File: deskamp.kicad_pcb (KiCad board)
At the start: 2 copper layers, 38 parts, among them J1 Input 01, J10 Input Select, J2 Input 02, J3 Preamp Out, J5 LFE, J6 Mute, J7 Sleep, J8 Motor, J9 Power, K1 TQ2-12V, K2 TQ2-12V, K3 TQ2-12V, K4 TQ2-12V, Q1 PN2222A, Q2 PN2222A, Q3 PN2222A, Q4 PN2222A, U1 esp32-wemos-d1-mini, U2 L9110, U3 TSR_1-2433

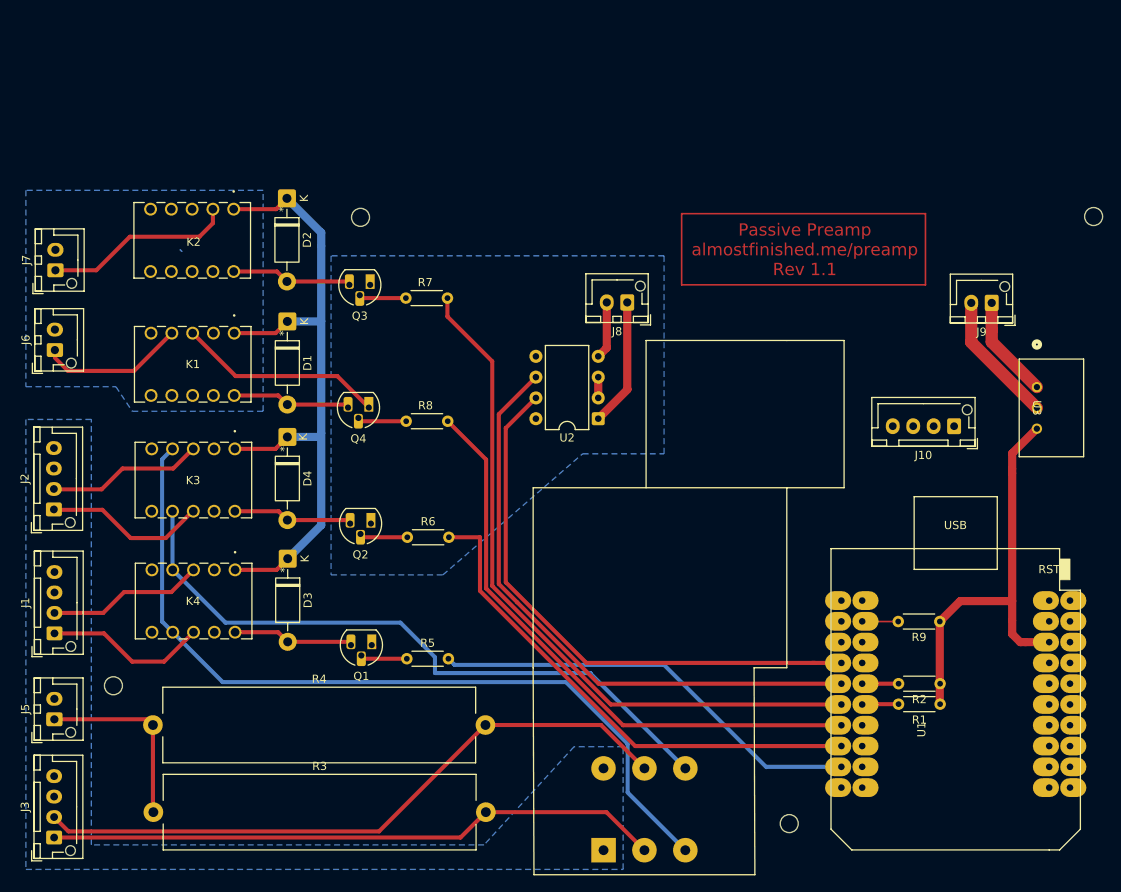
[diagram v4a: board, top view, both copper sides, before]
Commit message: Add board edge
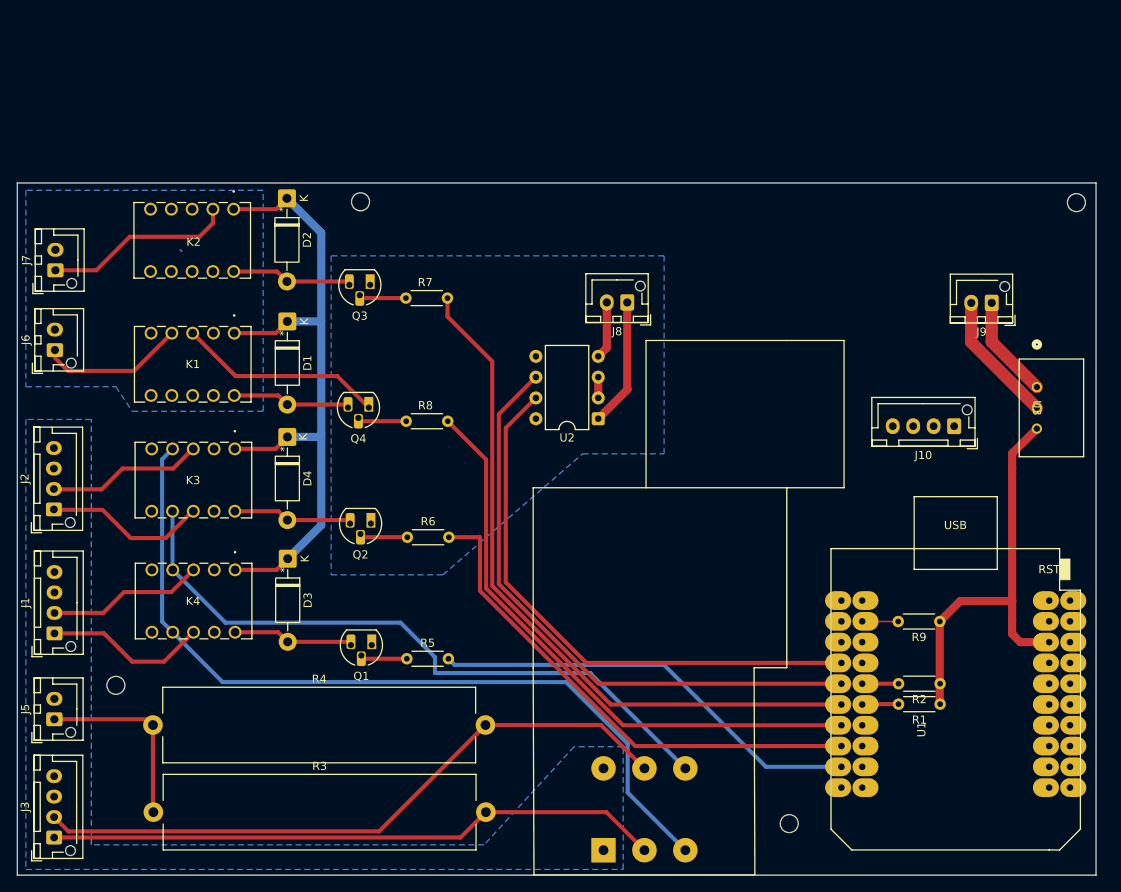
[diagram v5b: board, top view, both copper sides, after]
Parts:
- moved REF** 2.70 mm to (187.4, 65.5)
- moved REF** 1.90 mm to (99.9, 65.4)
- moved REF** 0.30 mm to (70.0, 124.5)
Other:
- board outline added: 131.9 x 84.6 mm
- board text removed: "Passive Preamp almostfinished.me/preamp Rev 1.1"

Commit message: Update deskamp.kicad_pcb
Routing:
- net +12V: track 96.7 -> 188.1 mm
- net GND: track 42.2 -> 131.4 mm
- net +3V3: track 54.0 -> 114.7 mm
- net Net-(J10-Pin_2): track 4.48 -> 40.2 mm
- net Net-(J10-Pin_3): track 4.44 -> 36.7 mm
- net Net-(J10-Pin_4): track 4.41 -> 28.6 mm
- net Net-(U1-IO_04): track 75.6 -> 74.1 mm
- net Net-(K3-Pad4): track 81.0 -> 79.9 mm

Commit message: Update deskamp.kicad_pcb
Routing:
- net Net-(J6-Pin_1): track 17.8 -> 15.2 mm
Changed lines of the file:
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@@
 			(at 2.54 1.92 0)
 			(layer "F.Fab")
+			(hide yes)
 			(effects
 				(font
@@
 			(at 2.54 1.92 0)
 			(layer "F.Fab")
+			(hide yes)
 			(effects
 				(font
@@
 	)
 	(segment
-		(start 167.29 68)
+		(start 89.583325 66.3)
+		(end 90.905825 64.9775)
+		(width 0.5)
+		(layer "F.Cu")
+		(net 1)
+	)
+	(segment
+		(start 90.905825 64.9775)
+		(end 94.928325 69)
+		(width 1)
+		(layer "F.Cu")
+		(net 1)
+	)
+	(segment
+		(start 168.29 69)
 		(end 177.045 77.755)
 		(width 1)
@@
 	)
 	(segment
-		(start 89.583325 66.3)
-		(end 90.905825 64.9775)
-		(width 0.5)
+		(start 94.928325 69)
+		(end 168.29 69)
+		(width 1)
 		(layer "F.Cu")
 		(net 1)
@@
 	)
 	(segment
-		(start 90.905825 64.9775)
-		(end 93.928325 68)
-		(width 1)
-		(layer "F.Cu")
-		(net 1)
-	)
-	(segment
 		(start 84.54 95.6)
 		(end 89.5 95.6)
@@
 	)
 	(segment
-		(start 93.928325 68)
-		(end 167.29 68)
-		(width 1)
-		(layer "F.Cu")
-		(net 1)
-	)
-	(segment
 		(start 95.1 69.171675)
 		(end 95.1 80)
@@
 	)
 	(segment
-		(start 174.545 77.755)
-		(end 169.245 77.755)
+		(start 149 98)
+		(end 127.425 98)
 		(width 1.5)
 		(layer "F.Cu")
@@
 	)
 	(segment
-		(start 149 98)
-		(end 127.425 98)
+		(start 169.245 77.755)
+		(end 149 98)
 		(width 1.5)
 		(layer "F.Cu")
@@
 	)
 	(segment
-		(start 174.545 82.568)
-		(end 174.545 77.755)
+		(start 174.545 77.755)
+		(end 169.245 77.755)
 		(width 1.5)
 		(layer "F.Cu")
@@
 	)
 	(segment
-		(start 169.245 77.755)
-		(end 149 98)
+		(start 174.545 82.568)
+		(end 174.545 77.755)
 		(width 1.5)
 		(layer "F.Cu")
@@
 	)
 	(segment
-		(start 72.219 86.071)
+		(start 74.77 83.52)
 		(end 76.84 81.45)
 		(width 0.5)
@@
 	)
 	(segment
-		(start 62.5427 84.464917)
-		(end 64.148783 86.071)
-		(width 0.5)
-		(layer "F.Cu")
-		(net 12)
-	)
-	(segment
 		(start 62.5427 83.52)
-		(end 62.5427 84.464917)
-		(width 0.2)
-		(layer "F.Cu")
-		(net 12)
-	)
-	(segment
-		(start 64.148783 86.071)
-		(end 72.219 86.071)
+		(end 74.77 83.52)
 		(width 0.5)
 		(layer "F.Cu")

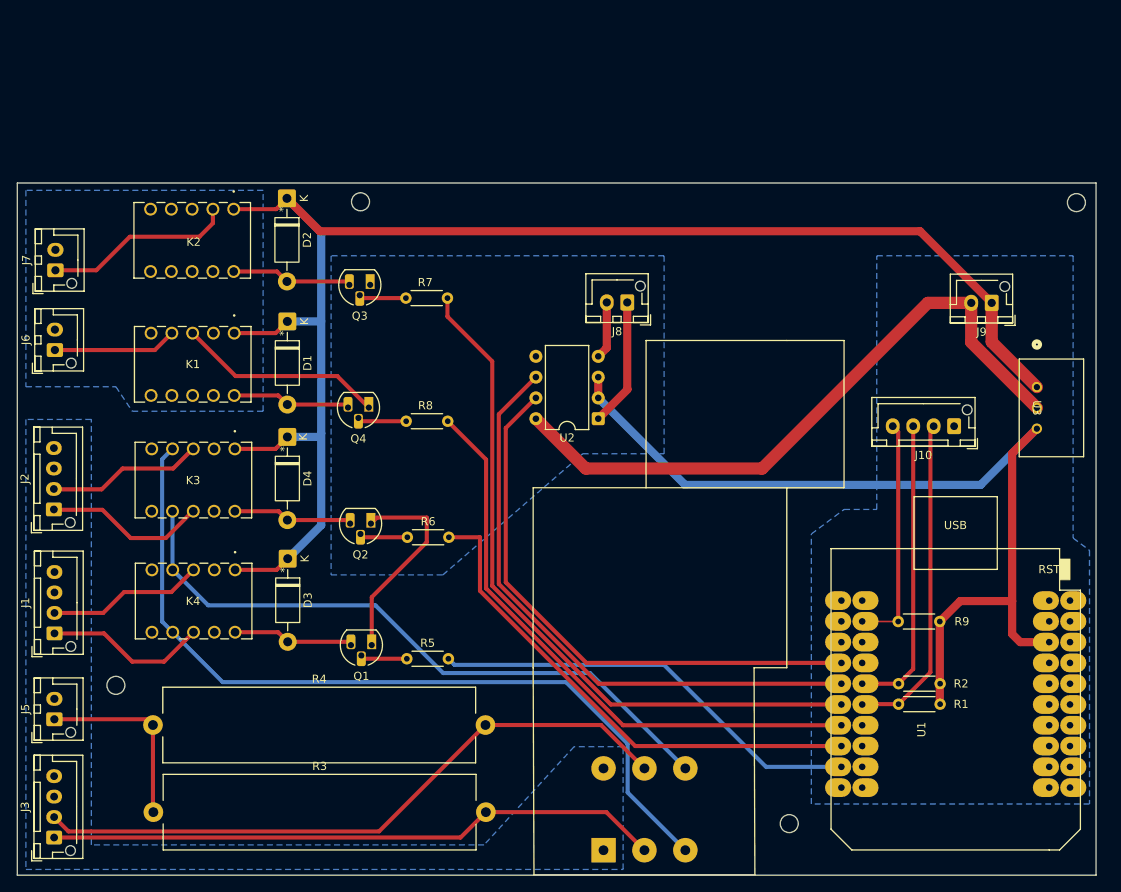
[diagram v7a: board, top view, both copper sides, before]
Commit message: Start afresh with layout
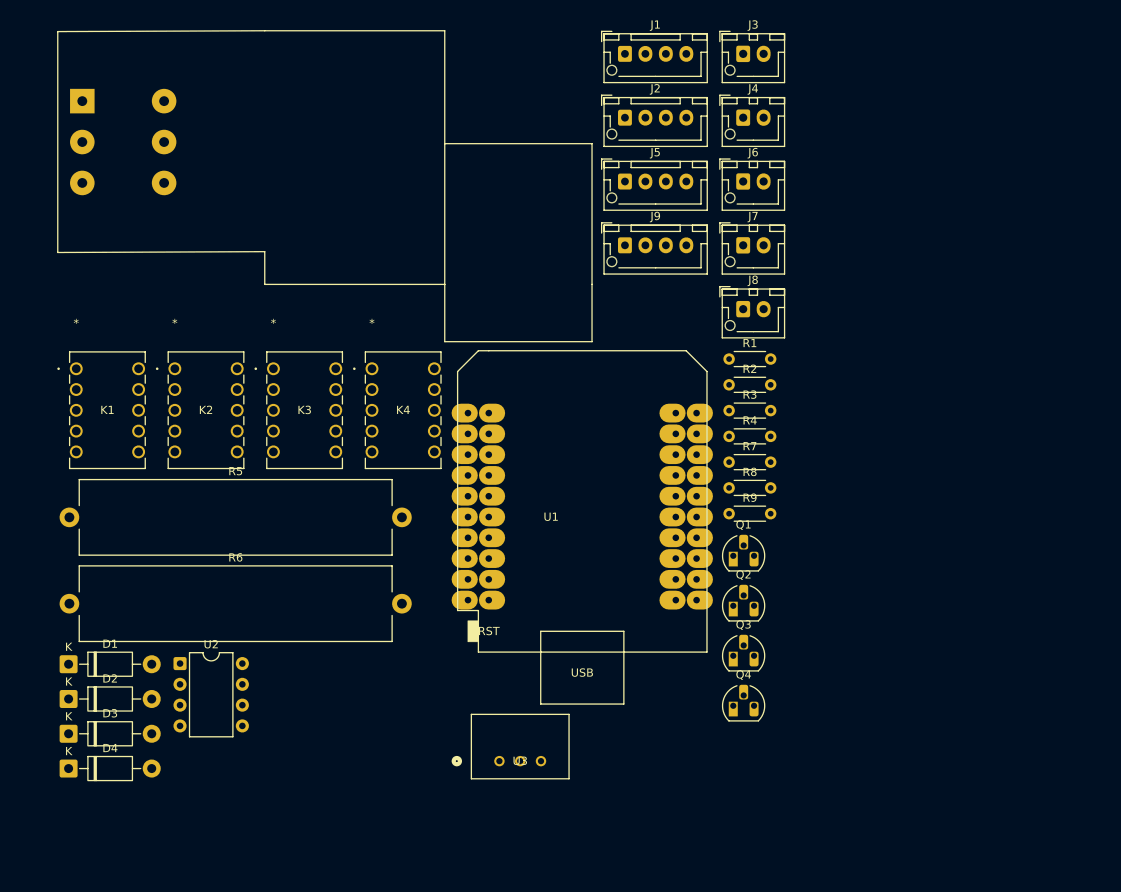
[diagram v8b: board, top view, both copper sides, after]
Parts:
- removed J10: Input Select, Connector_JST:JST_XH_B4B-XH-AM_1x04_P2.50mm_Vertical
- removed REF** (x4): MountingHole_2.2mm_M2_DIN965, MountingHole:MountingHole_2.2mm_M2_DIN965
- added J4: Mute, Connector_JST:JST_XH_B2B-XH-AM_1x02_P2.50mm_Vertical, F.Cu at (146.7, 55.1)
- J3: value Preamp Out -> Sleep; footprint Connector_JST:JST_XH_B4B-XH-AM_1x04_P2.50mm_Vertical -> Connector_JST:JST_XH_B2B-XH-AM_1x02_P2.50mm_Vertical
- J5: value LFE -> Preamp Out; footprint Connector_JST:JST_XH_B2B-XH-AM_1x02_P2.50mm_Vertical -> Connector_JST:JST_XH_B4B-XH-AM_1x04_P2.50mm_Vertical
- J6: value Mute -> LFE
- J7: value Sleep -> Power
- J9: value Power -> Input Select; footprint Connector_JST:JST_XH_B2B-XH-AM_1x02_P2.50mm_Vertical -> Connector_JST:JST_XH_B4B-XH-AM_1x04_P2.50mm_Vertical
- R1, R2: value 10K -> 1K
- R3, R4: value 10K -> 1K; footprint Resistor_THT:R_Axial_Power_L38.0mm_W9.0mm_P40.64mm -> Resistor_THT:R_Axial_DIN0204_L3.6mm_D1.6mm_P5.08mm_Horizontal
- R5, R6: value 1K -> 10K; footprint Resistor_THT:R_Axial_DIN0204_L3.6mm_D1.6mm_P5.08mm_Horizontal -> Resistor_THT:R_Axial_Power_L38.0mm_W9.0mm_P40.64mm
- R7, R8: value 1K -> 10K
- moved J3 127.5 mm to (146.7, 47.3), turned to 0 degrees
- moved RV1 112.9 mm to (64.9, 53.1), turned to 0 degrees
- moved J1 99.4 mm to (132.2, 47.3), turned to 0 degrees
- moved J5 95.8 mm to (132.2, 62.9), turned to 0 degrees
- moved J6 86.6 mm to (146.7, 62.9), turned to 0 degrees
- moved R3 85.8 mm to (144.9, 90.9)
- moved J2 84.6 mm to (132.2, 55.1), turned to 0 degrees
- moved J7 84.1 mm to (146.7, 70.7), turned to 0 degrees
- moved U3 80.0 mm to (116.9, 133.8), turned to 0 degrees
- moved R4 78.8 mm to (144.9, 94.1)
- moved D2 66.8 mm to (64.2, 126.2), turned to 0 degrees
- moved Q3 63.4 mm to (145.5, 120.9), turned to 0 degrees
- moved U2 59.2 mm to (77.8, 121.8), turned to 0 degrees
- moved Q4 57.6 mm to (145.5, 127.0), turned to 0 degrees
- moved U1 51.1 mm to (127.0, 102.7), turned to 0 degrees
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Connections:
- J3 pad 2: Net-(J3-Pin_2) -> GND
- J5 pad 2: GNDA -> Net-(J5-Pin_2)
- J6 pad 2: GND -> GNDA
- J7 pad 1: Net-(J7-Pin_1) -> +12V
- J9 pad 1: +12V -> GND
- J9 pad 2: GND -> Net-(J9-Pin_2)
- K1 pad 3: GND -> Net-(J1-Pin_2)
- K1 pad 4: Net-(J6-Pin_1) -> Net-(K1-Pad4)
- K1 pad 7: unconnected-(K1-Pad7) -> Net-(K1-Pad7)
- K1 pad 8: unconnected-(K1-Pad8) -> Net-(J1-Pin_1)
- K2 pad 2: Net-(J7-Pin_1) -> unconnected-(K2-Pad2)
- K2 pad 3: GND -> Net-(J2-Pin_2)
- K2 pad 4: unconnected-(K2-Pad4) -> Net-(K1-Pad7)
- K2 pad 7: unconnected-(K2-Pad7) -> Net-(K1-Pad4)
- K2 pad 8: unconnected-(K2-Pad8) -> Net-(J2-Pin_1)
- K3 pad 2: unconnected-(K3-Pad2) -> Net-(J3-Pin_1)
- K3 pad 3: Net-(J1-Pin_2) -> GND
- K3 pad 4: Net-(K3-Pad4) -> unconnected-(K3-Pad4)
- K3 pad 7: Net-(K3-Pad7) -> unconnected-(K3-Pad7)
- K3 pad 8: Net-(J1-Pin_1) -> unconnected-(K3-Pad8)
- K4 pad 3: Net-(J2-Pin_2) -> GND
- K4 pad 4: Net-(K3-Pad7) -> Net-(J4-Pin_1)
- K4 pad 7: Net-(K3-Pad4) -> unconnected-(K4-Pad7)
- K4 pad 8: Net-(J2-Pin_1) -> unconnected-(K4-Pad8)
- Q1 pad 3: Net-(D3-A) -> Net-(D1-A)
- Q2 pad 3: Net-(D4-A) -> Net-(D2-A)
- Q3 pad 3: Net-(D2-A) -> Net-(D3-A)
- Q4 pad 3: Net-(D1-A) -> Net-(D4-A)
- R1 pad 1: +3V3 -> Net-(Q1-B)
- R1 pad 2: Net-(J10-Pin_2) -> unconnected-(R1-Pad2)
- R2 pad 1: +3V3 -> Net-(Q2-B)
- R2 pad 2: Net-(J10-Pin_3) -> unconnected-(R2-Pad2)
- R3 pad 1: Net-(J5-Pin_1) -> Net-(Q3-B)
- R3 pad 2: Net-(J3-Pin_1) -> unconnected-(R3-Pad2)
- R4 pad 1: Net-(J5-Pin_1) -> Net-(Q4-B)
- R4 pad 2: Net-(J3-Pin_2) -> unconnected-(R4-Pad2)
- R5 pad 1: Net-(Q1-B) -> Net-(J6-Pin_1)
- R5 pad 2: Net-(U1-IO_27) -> Net-(J5-Pin_1)
- R6 pad 1: Net-(Q2-B) -> Net-(J6-Pin_1)
- R6 pad 2: Net-(U1-IO_25) -> Net-(J5-Pin_2)
- R7 pad 1: Net-(Q3-B) -> +3V3
- R7 pad 2: Net-(U1-IO_12/TDI) -> Net-(J9-Pin_4)
- R8 pad 1: Net-(Q4-B) -> +3V3
- R8 pad 2: Net-(U1-IO_32) -> Net-(J9-Pin_3)
- R9 pad 2: Net-(J10-Pin_4) -> Net-(J9-Pin_2)
- RV1 pad 1: Net-(K3-Pad7) -> Net-(K1-Pad7)
- RV1 pad 2: Net-(J3-Pin_1) -> Net-(J5-Pin_1)
- RV1 pad 4: Net-(K3-Pad4) -> Net-(K1-Pad4)
- RV1 pad 5: Net-(J3-Pin_2) -> Net-(J5-Pin_2)
- U1 pad 24: Net-(U1-IO_27) -> unconnected-(U1-IO_27-Pad24)
- U1 pad 26: Net-(U1-IO_25) -> unconnected-(U1-IO_25-Pad26)
- U1 pad 28: Net-(U1-IO_32) -> unconnected-(U1-IO_32-Pad28)
- U1 pad 29: Net-(J10-Pin_2) -> unconnected-(U1-IO_17/D3-Pad29)
- U1 pad 30: Net-(U1-IO_12/TDI) -> unconnected-(U1-IO_12/TDI-Pad30)
- U1 pad 31: Net-(J10-Pin_3) -> unconnected-(U1-IO_16/D4-Pad31)
- U1 pad 37: Net-(J10-Pin_4) -> unconnected-(U1-TD0-Pad37)
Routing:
- net +12V: track 188.1 -> 0.00 mm
- net GND: track 131.4 -> 0.00 mm
- net +3V3: track 114.7 -> 0.00 mm
- net Net-(K3-Pad7): track 100.6 -> 0.00 mm
- net Net-(U1-IO_12/TDI): track 86.1 -> 0.00 mm
- net Net-(J3-Pin_2): track 80.5 -> 0.00 mm
- net Net-(K3-Pad4): track 79.9 -> 0.00 mm
- net Net-(J3-Pin_1): track 75.4 -> 0.00 mm
- net Net-(U1-IO_04): track 74.1 -> 0.00 mm
- net Net-(U1-IO_32): track 72.7 -> 0.00 mm
- net Net-(U1-IO_00): track 69.2 -> 0.00 mm
- net Net-(U1-IO_25): track 62.4 -> 0.00 mm
- net Net-(U1-IO_27): track 53.5 -> 0.00 mm
- net Net-(J10-Pin_2): track 40.2 -> 0.00 mm
- net Net-(J10-Pin_3): track 36.7 -> 0.00 mm
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- removed copper zone on B.Cu, net GND
- removed copper zone on B.Cu, net GNDA
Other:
- board outline removed
